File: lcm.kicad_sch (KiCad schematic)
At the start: 13 parts, among them J6 F52R-1A7H1-11020, U10 NTS0102GT

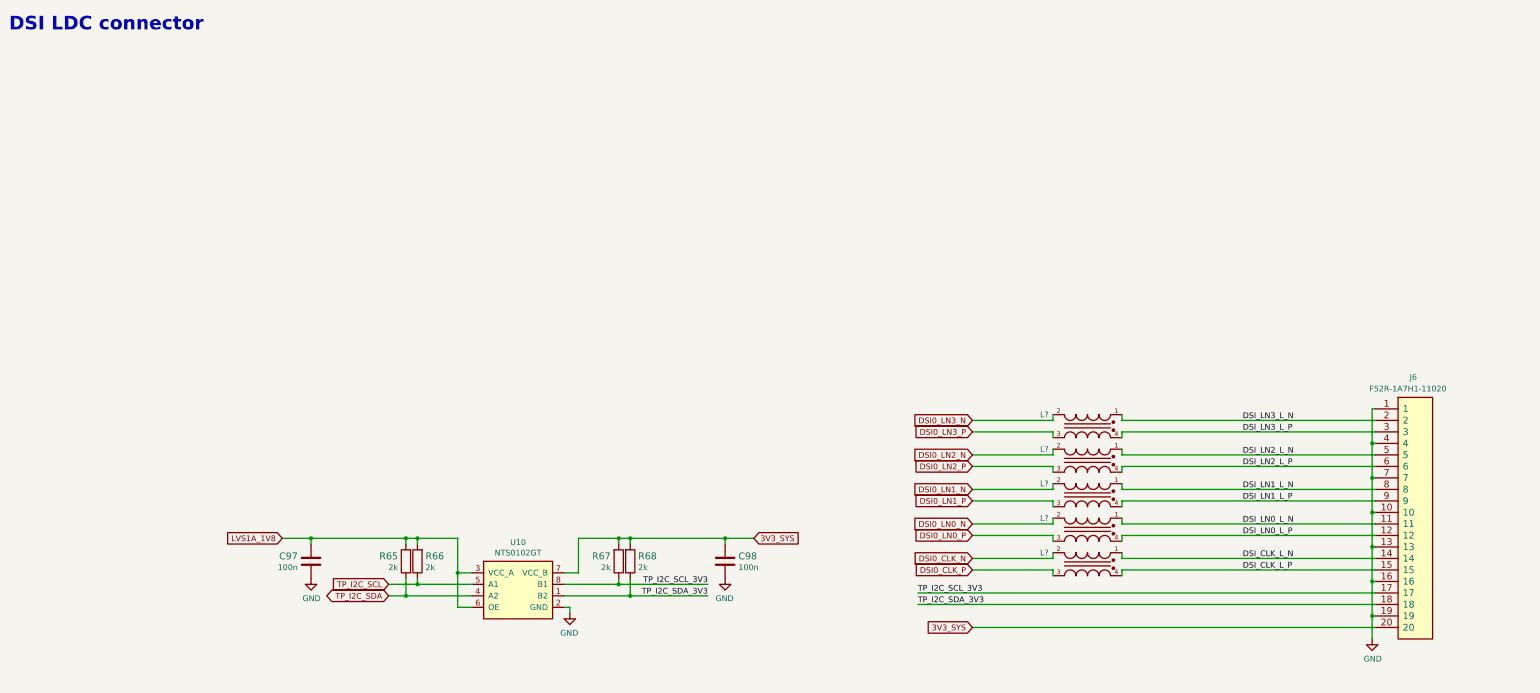
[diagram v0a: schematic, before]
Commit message: Introduce component standardization
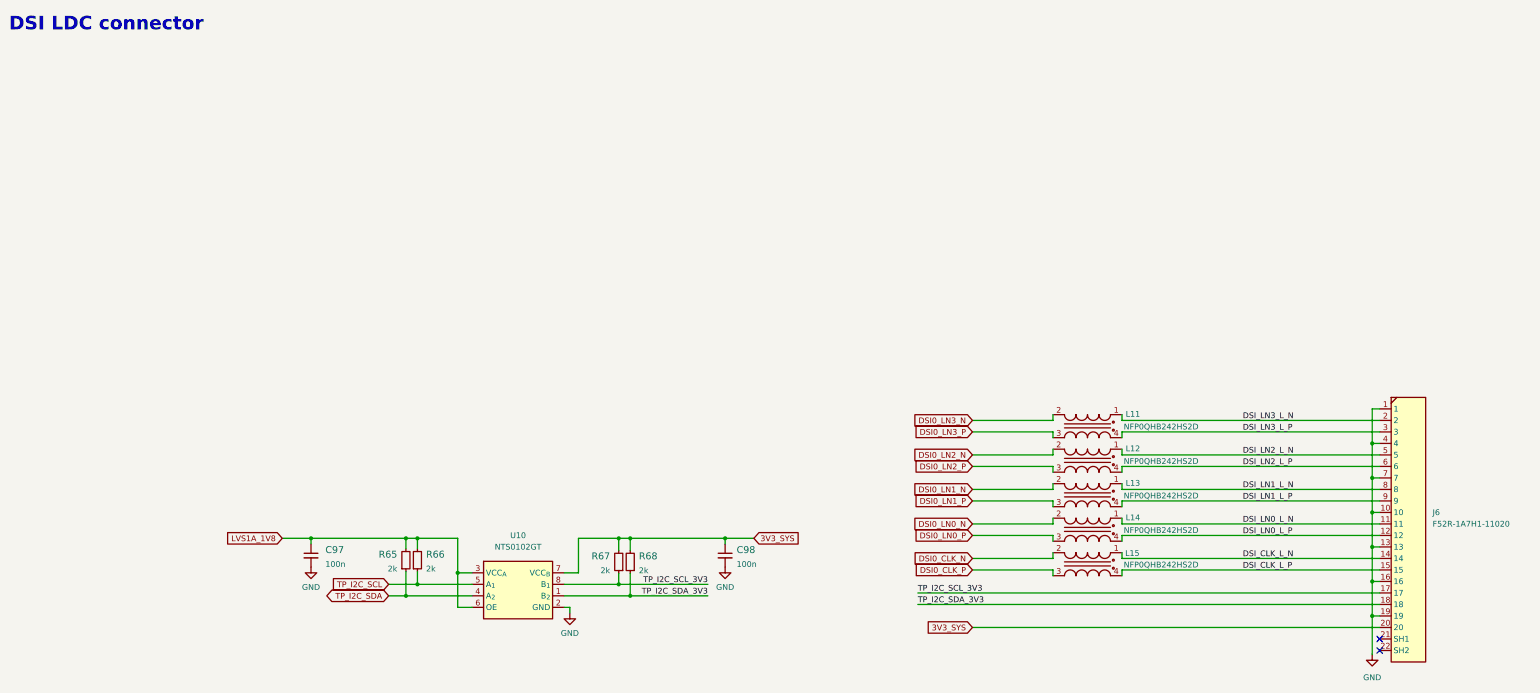
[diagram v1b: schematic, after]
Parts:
- C97, C98: footprint sa800u-baseboard-hw-footprints:0402-cap -> sa800u-baseboard-hw-footprints:C_0402_1005Metric; Author (none) -> Antmicro; Dielectric (none) -> X5R; License (none) -> Apache-2.0; Voltage (none) -> 50V
- J6: Author (none) -> Antmicro; License (none) -> Apache-2.0; Manufacturer AMPHENOL ICC -> Amphenol
- L11, L12, L13, L14, L15: renamed from L?; value (none) -> NFP0QHB242HS2D; footprint (none) -> sa800u-baseboard-hw-footprints:L_Murata_025020_0605Metric; Author (none) -> Antmicro; License (none) -> Apache-2.0; Manufacturer MURATA -> Murata
- R65, R66, R67, R68: footprint sa800u-baseboard-hw-footprints:0402-res -> sa800u-baseboard-hw-footprints:R_0402_1005Metric; Author (none) -> Antmicro; License (none) -> Apache-2.0; MPN CRCW04022K00FKED -> CR0402-FX-2001GLF; Manufacturer VISHAY -> Bourns; Tolerance (none) -> 1%
- U10: value NTS0102GT -> NTS0102_XSON; footprint sa800u-baseboard-hw-footprints:PSON50P100X195X50-8N -> sa800u-baseboard-hw-footprints:XSON-8_1x1.95mm_P0.5mm; symbol sa800u-baseboard-hw:NTS0102GT -> sa800u-baseboard-hw:NTS0102_XSON; Author (none) -> Antmicro; License (none) -> Apache-2.0; Manufacturer NXP Semiconductors -> NXP
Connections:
- no-connect marks 0 -> 2
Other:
- moved on the sheet: C97, C98

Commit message: Add OHP assets
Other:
- company: (none) -> Antmicro Ltd.
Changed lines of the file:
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@@
   (title_block
     (title "SA800U (Snapdragon 845) Baseboard")
-    (date "2023-07-27")
-    (rev "1.0.2")
+    (date "2023-10-19")
+    (rev "1.0.3")
+    (company "Antmicro Ltd.")
     (comment 1 "www.antmicro.com")
-    (comment 2 "Antmicro Ltd.")
   )
   (junction (at 314.325 116.84) (diameter 0) (color 0 0 0 0)
@@
     (pin "1")
   )
-  (symbol (lib_id "sa800u-baseboard-hw:NFP0QHB242HS2D") (at 259.08 102.87 0) (mirror y) (unit 1)
+  (symbol (lib_name "NFP0QHB242HS2D_2") (lib_id "sa800u-baseboard-hw:NFP0QHB242HS2D") (at 259.08 102.87 0) (mirror y) (unit 1)
     (in_bom yes) (on_board yes)
     (property "Reference" "L11" (id 0) (at 261.493 102.743 0))
@@
     (pin "4")
   )
-  (symbol (lib_id "sa800u-baseboard-hw:NFP0QHB242HS2D") (at 259.08 110.49 0) (mirror y) (unit 1)
+  (symbol (lib_name "NFP0QHB242HS2D_3") (lib_id "sa800u-baseboard-hw:NFP0QHB242HS2D") (at 259.08 110.49 0) (mirror y) (unit 1)
     (in_bom yes) (on_board yes)
     (property "Reference" "L12" (id 0) (at 261.493 110.363 0))
@@
     (pin "4")
   )
-  (symbol (lib_id "sa800u-baseboard-hw:NFP0QHB242HS2D") (at 259.08 125.73 0) (mirror y) (unit 1)
+  (symbol (lib_name "NFP0QHB242HS2D_4") (lib_id "sa800u-baseboard-hw:NFP0QHB242HS2D") (at 259.08 125.73 0) (mirror y) (unit 1)
     (in_bom yes) (on_board yes)
     (property "Reference" "L14" (id 0) (at 261.493 125.603 0))
@@
     (pin "4")
   )
-  (symbol (lib_id "sa800u-baseboard-hw:NFP0QHB242HS2D") (at 259.08 133.35 0) (mirror y) (unit 1)
+  (symbol (lib_name "NFP0QHB242HS2D_1") (lib_id "sa800u-baseboard-hw:NFP0QHB242HS2D") (at 259.08 133.35 0) (mirror y) (unit 1)
     (in_bom yes) (on_board yes)
     (property "Reference" "L15" (id 0) (at 261.366 133.477 0))
